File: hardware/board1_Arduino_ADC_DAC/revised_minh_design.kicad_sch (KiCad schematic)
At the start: 36 parts, among them J1 Conn_01x03_Male, J2 Conn_02x08_Odd_Even, J3 Conn_02x08_Odd_Even, J4 Conn_02x08_Odd_Even, J5 Conn_01x02_Male, U1 ESP32-DevKit-C, U2 LM7805_TO220, U3 MCP1754S-3302xCB, U4 MCP1825S-3.3V, U5 MCP1501-33xSN, U6 MCP3464R, U7 MCP3464R, U8 DAC8568IAPW, X1 ECS-2520MVLC-049-BN-TR

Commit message: cleanup
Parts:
- added C19, C21: 10uF, Capacitor_SMD:C_0805_2012Metric_Pad1.18x1.45mm_HandSolder, symbol Device:C
- added C20, C22: 0.1uF, Capacitor_SMD:C_0805_2012Metric_Pad1.18x1.45mm_HandSolder, symbol Device:C
- added R4: 0, Resistor_SMD:R_0805_2012Metric_Pad1.20x1.40mm_HandSolder, symbol Device:R
- added R5, R6: 100k, Resistor_SMD:R_0805_2012Metric_Pad1.20x1.40mm_HandSolder, symbol Device:R
- added TP1: TestPoint, Connector_PinHeader_2.54mm:PinHeader_1x01_P2.54mm_Vertical, symbol Connector:TestPoint
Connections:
- net +3.3VDAC: now also C19.1, C20.1, C21.1, C22.1
- net +3V3: now also R5.2, R6.1
- net Earth: now also C19.2, C20.2, C21.2, C22.2
- net VoutB: now also J4.13 (Pin_13); no longer J4.1 (Pin_1)
- net VoutC: now also J4.11 (Pin_11); no longer J4.13 (Pin_13)
- net VoutD: now also J4.9 (Pin_9); no longer J4.3 (Pin_3)
- net VoutE: now also J4.7 (Pin_7); no longer J4.11 (Pin_11)
- net VoutG: now also J4.3 (Pin_3); no longer J4.9 (Pin_9)
- net VoutH: now also J4.1 (Pin_1); no longer J4.7 (Pin_7)
- net at X1.3 (OUT): now also R3.2, R4.2, TP1.1; no longer R3.1
- net MDAT2: now reaches A1.22 (A3)
- net MDAT2: now also U1.28 (25), U7.17 (~{IRQ}/MDAT), R6.2
- removed net CLK: R3.2, U6.18 (MLCK), U7.18 (MLCK)
- net MDAT renamed MDAT1
- net MDAT1: now also R5.1; no longer U7.17 (~{IRQ}/MDAT)
- net SI renamed PI
- net PI: now also U8.15 (D_{IN})
- net SO renamed PO
- net PO: no longer U8.15 (D_{IN})
- new net ADC_CLK1: R4.1, U6.18 (MLCK)
- new net ADC_CLK2: R3.1, U7.18 (MLCK)
- no-connect marks 31 -> 29
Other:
- note removed: "MOSI"
- title: (none) -> S.H.V.R.I.M.P.S.    16 channels data acquisition device
- moved on the sheet: A1, C10, C11, C12, C13, C14, C15, C16, C17, C18, C3, C4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

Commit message: routed the netlist for ADC/DAC v2
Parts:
- added D1: SM4004, Diode_SMD:D_MELF, symbol Diode:SM4004
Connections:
- net +12V: now also D1.1 (K); no longer J1.1 (Pin_1)
- net ADC1_1: now also J2.2 (Pin_2); no longer J2.1 (Pin_1)
- net ADC1_2: now also J2.4 (Pin_4); no longer J2.3 (Pin_3)
- net ADC1_3: now also J2.6 (Pin_6); no longer J2.5 (Pin_5)
- net ADC1_4: now also J2.8 (Pin_8); no longer J2.7 (Pin_7)
- net ADC1_5: now also J2.10 (Pin_10); no longer J2.9 (Pin_9)
- net ADC1_6: now also J2.12 (Pin_12); no longer J2.11 (Pin_11)
- net ADC1_7: now also J2.14 (Pin_14); no longer J2.13 (Pin_13)
- net ADC1_8: now also J2.16 (Pin_16); no longer J2.15 (Pin_15)
- net ADC2_1: now also J3.2 (Pin_2); no longer J3.1 (Pin_1)
- net ADC2_2: now also J3.4 (Pin_4); no longer J3.3 (Pin_3)
- net ADC2_3: now also J3.6 (Pin_6); no longer J3.5 (Pin_5)
- net ADC2_4: now also J3.8 (Pin_8); no longer J3.7 (Pin_7)
- net ADC2_5: now also J3.10 (Pin_10); no longer J3.9 (Pin_9)
- net ADC2_6: now also J3.12 (Pin_12); no longer J3.11 (Pin_11)
- net ADC2_7: now also J3.14 (Pin_14); no longer J3.13 (Pin_13)
- net ADC2_8: now also J3.16 (Pin_16); no longer J3.15 (Pin_15)
- net Earth: now also J2.1 (Pin_1), J2.11 (Pin_11), J2.13 (Pin_13), J2.15 (Pin_15), J2.3 (Pin_3), J2.5 (Pin_5), J2.7 (Pin_7), J2.9 (Pin_9), J3.1 (Pin_1), J3.11 (Pin_11), J3.13 (Pin_13), J3.15 (Pin_15), J3.3 (Pin_3), J3.5 (Pin_5), J3.7 (Pin_7), J3.9 (Pin_9); no longer J2.10 (Pin_10), J2.12 (Pin_12), J2.14 (Pin_14), J2.16 (Pin_16), J2.2 (Pin_2), J2.4 (Pin_4), J2.6 (Pin_6), J2.8 (Pin_8), J3.10 (Pin_10), J3.12 (Pin_12), J3.14 (Pin_14), J3.16 (Pin_16), J3.2 (Pin_2), J3.4 (Pin_4), J3.6 (Pin_6), J3.8 (Pin_8)
- new net: D1.2 (A), J1.1 (Pin_1)
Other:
- moved on the sheet: J1

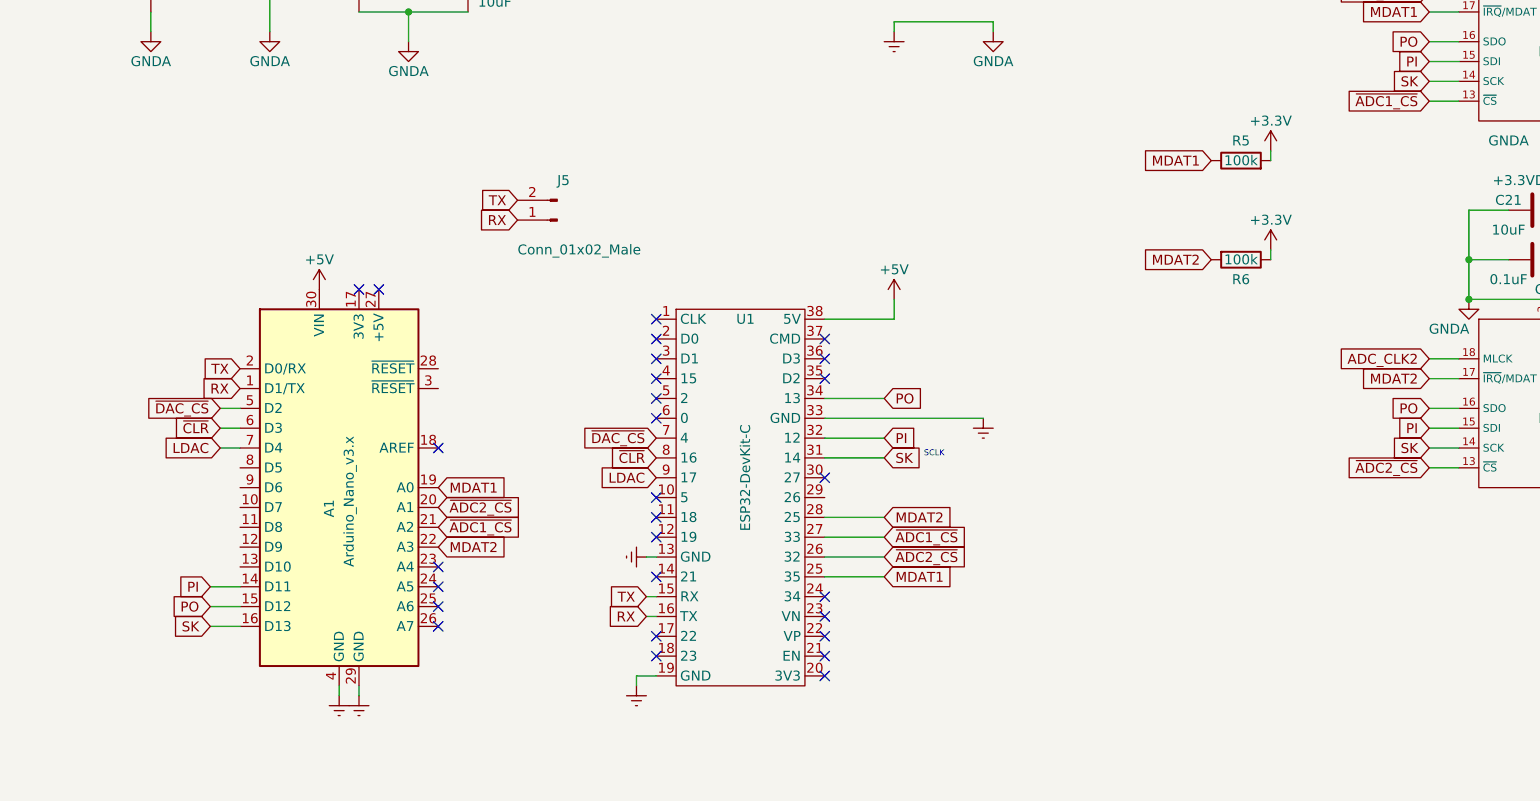
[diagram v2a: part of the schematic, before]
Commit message: hardware update to add GPIO directly to MCU
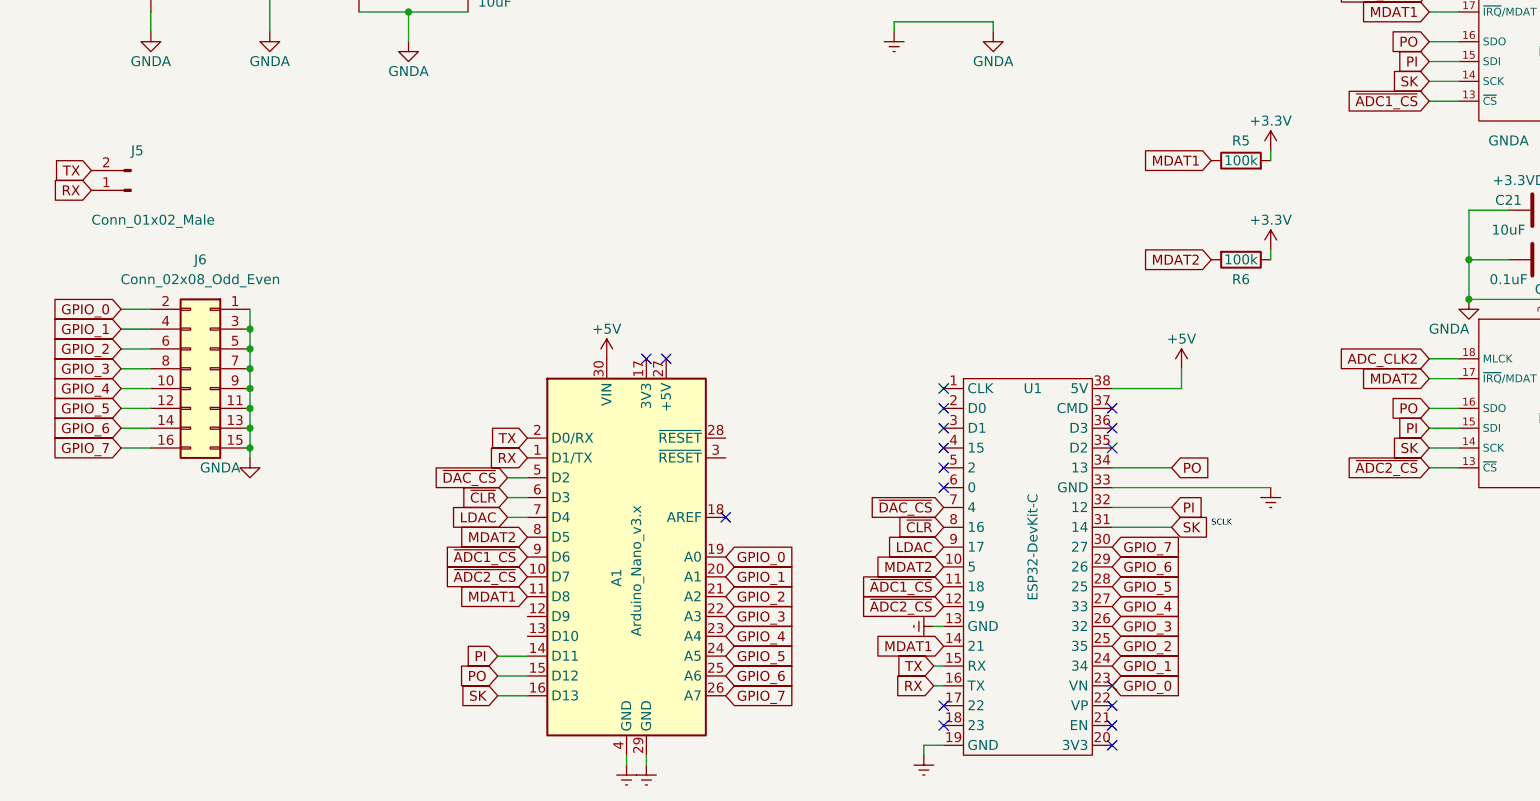
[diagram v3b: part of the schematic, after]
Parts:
- added J6: Conn_02x08_Odd_Even, Connector_PinSocket_2.54mm:PinSocket_2x08_P2.54mm_Vertical, symbol Connector_Generic:Conn_02x08_Odd_Even
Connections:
- net Earth: now also J6.1 (Pin_1), J6.11 (Pin_11), J6.13 (Pin_13), J6.15 (Pin_15), J6.3 (Pin_3), J6.5 (Pin_5), J6.7 (Pin_7), J6.9 (Pin_9)
- net MDAT1: now also A1.11 (D8), U1.14 (21); no longer A1.19 (A0), U1.25 (35)
- net MDAT2: now also A1.8 (D5), U1.10 (5); no longer A1.22 (A3), U1.28 (25)
- net ~{ADC1_CS}: now also A1.9 (D6), U1.11 (18); no longer A1.21 (A2), U1.27 (33)
- net ~{ADC2_CS}: now also A1.10 (D7), U1.12 (19); no longer A1.20 (A1), U1.26 (32)
- net GPIO_4: now reaches A1.23 (A4)
- net GPIO_4: now also U1.27 (33), J6.10 (Pin_10)
- net GPIO_5: now reaches A1.24 (A5)
- net GPIO_5: now also U1.28 (25), J6.12 (Pin_12)
- net GPIO_6: now reaches A1.25 (A6)
- net GPIO_6: now also U1.29 (26), J6.14 (Pin_14)
- net GPIO_7: now reaches A1.26 (A7)
- net GPIO_7: now also U1.30 (27), J6.16 (Pin_16)
- net GPIO_0: now reaches U1.23 (VN)
- net GPIO_0: now also A1.19 (A0), J6.2 (Pin_2)
- net GPIO_1: now reaches U1.24 (34)
- net GPIO_1: now also A1.20 (A1), J6.4 (Pin_4)
- new net GPIO_2: A1.21 (A2), J6.6 (Pin_6), U1.25 (35)
- new net GPIO_3: A1.22 (A3), J6.8 (Pin_8), U1.26 (32)
- no-connect marks 29 -> 19
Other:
- moved on the sheet: A1, J5, U1
